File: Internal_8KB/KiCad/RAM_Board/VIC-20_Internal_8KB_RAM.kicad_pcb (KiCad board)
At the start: 2 copper layers, 70 x 60 mm, 10 parts, among them J1 UD4, J2 UE4, J3 Switch, J4 RAM Signals, U1 6264, U2 GAL16V8

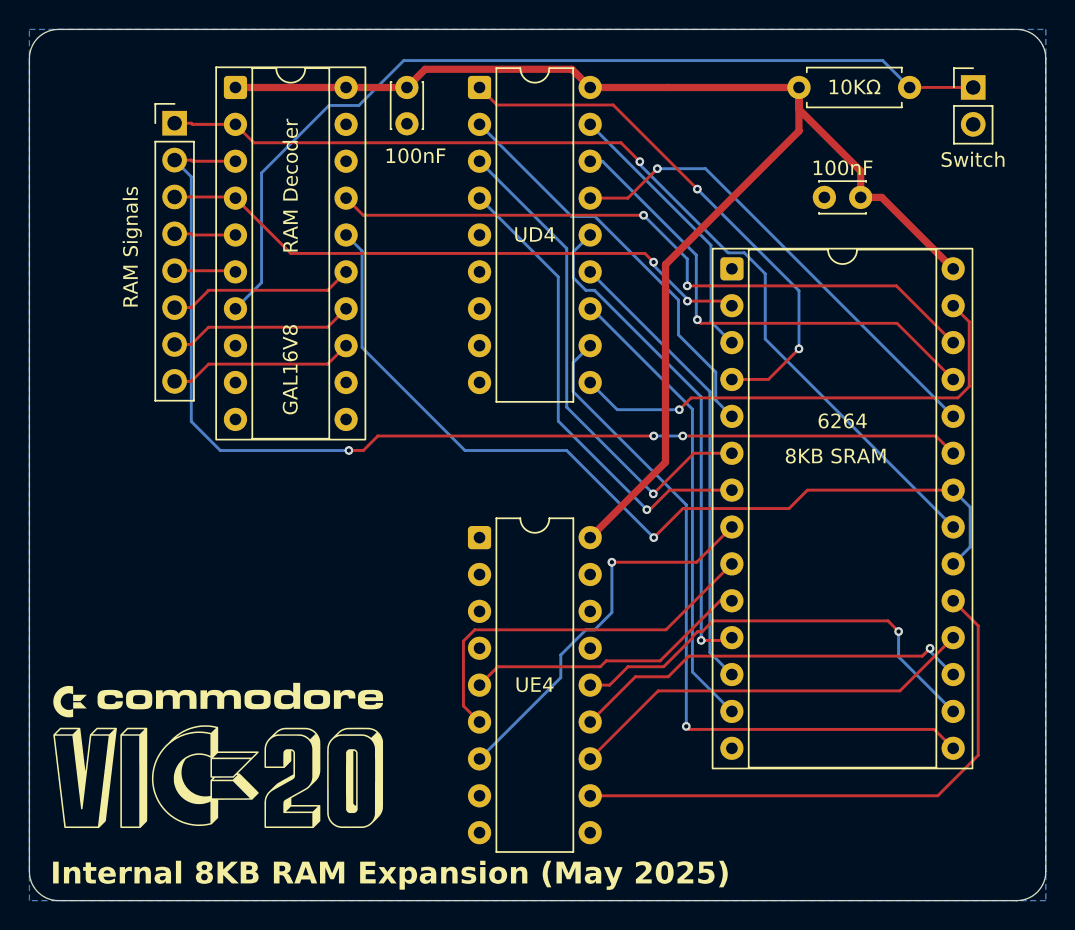
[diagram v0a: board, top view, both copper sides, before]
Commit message: Rename VIC20 to VIC-20
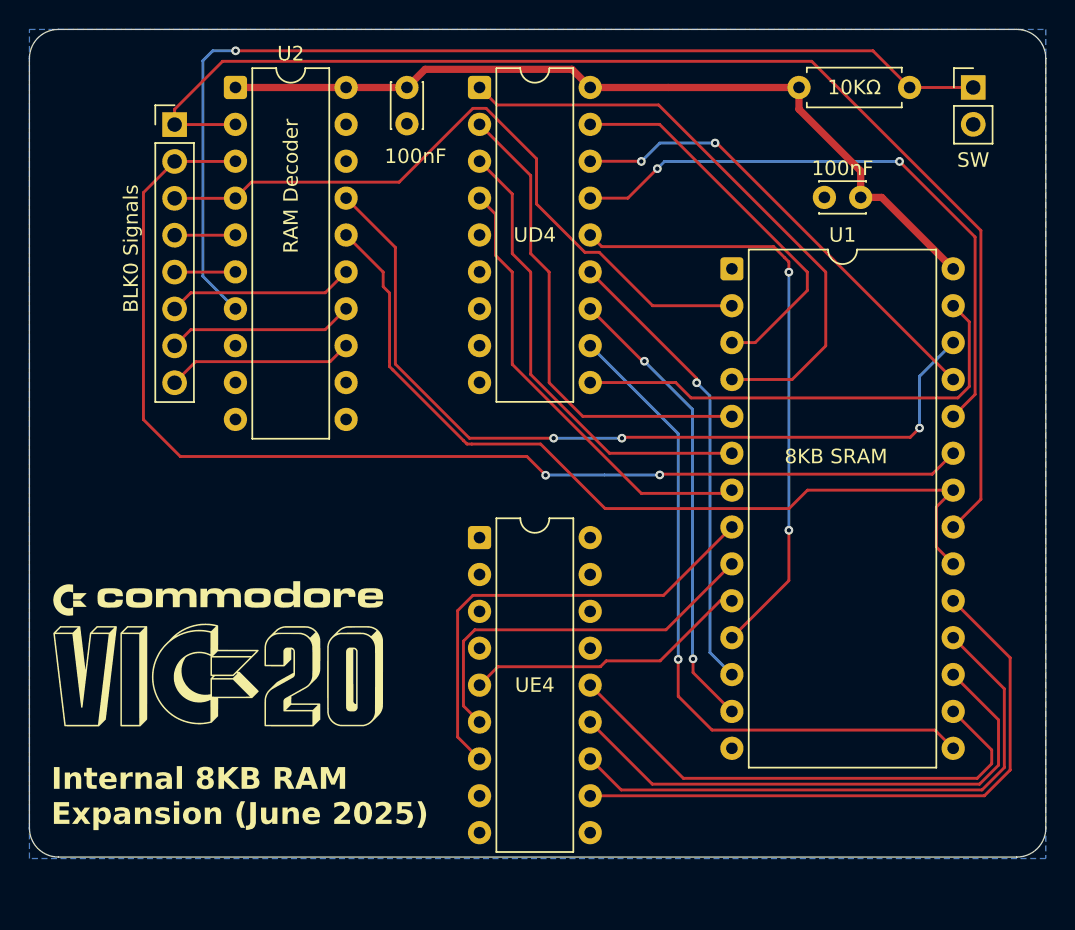
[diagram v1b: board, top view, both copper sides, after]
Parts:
- J3: value Switch -> SW
- J4: value RAM Signals -> BLK0 Signals
- U1: footprint Package_DIP:DIP-28_W15.24mm_Socket -> Package_DIP:DIP-28_W15.24mm
- U2: footprint Package_DIP:DIP-20_W7.62mm_Socket -> Package_DIP:DIP-20_W7.62mm
- moved G*** 7.00 mm to (62.0, 74.1)
- moved J4 0.09 mm to (59.0, 37.7)
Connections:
- J2 pad 18: +5V -> unconnected-(J2-Pin_18-Pad18)
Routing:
- net +5V: track 94.5 -> 57.6 mm
- net VA10: track 67.9 -> 88.2 mm, vias 1 -> 0
- net BD6: track 28.5 -> 40.5 mm
- net CS2: track 47.0 -> 58.2 mm, vias 2 -> 3
- net BD5: track 28.0 -> 38.0 mm, vias 1 -> 0
- net VA9: track 32.9 -> 42.7 mm, vias 1 -> 2
- net S: track 63.1 -> 72.4 mm, vias 0 -> 1
- net VA7: track 19.1 -> 27.1 mm
- net BD0: track 34.6 -> 42.2 mm, vias 1 -> 2
- net VA12: track 41.7 -> 49.0 mm, vias 2 -> 0
- net VA2: track 26.9 -> 32.1 mm, vias 1 -> 0
- net VA5: track 28.2 -> 33.3 mm
- net BD4: track 30.5 -> 35.4 mm, vias 1 -> 0
- net VA6: track 37.3 -> 41.6 mm, vias 2 -> 0
- net VA11: track 76.9 -> 80.9 mm, vias 3 -> 2
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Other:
- board size 70 x 60 mm -> 70 x 57 mm
- board text added: "Internal 8KB RAM Expansion (June 2025)"
- board text removed: "Internal 8KB RAM Expansion (May 2025)"
